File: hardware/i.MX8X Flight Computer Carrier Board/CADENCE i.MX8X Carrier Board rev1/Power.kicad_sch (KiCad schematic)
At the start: 64 parts, among them U1 LT8612, U2 LT8612, U3 TPS22975, U4 LT3115-1, U5 TLV71325PDQNR, U6 TLV71310PDQNR

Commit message: updated power schematic footprints for imx8x
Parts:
- U1, U2: footprint footprints:QFN-28_UDE_LTI -> LT8612:QFN-28_UDE_LTI
- U3: footprint (none) -> Footprints:DSG0008B
- U4: footprint (none) -> LTC3115EFE-1:CONV_LTC3115EFE-1_PBF
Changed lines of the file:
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@@
 			)
 		)
-		(property "Footprint" "footprints:QFN-28_UDE_LTI"
+		(property "Footprint" "LT8612:QFN-28_UDE_LTI"
 			(at 86.36 29.21 0)
 			(effects
@@
 			)
 		)
-		(property "Footprint" ""
+		(property "Footprint" "LTC3115EFE-1:CONV_LTC3115EFE-1_PBF"
 			(at 224.79 134.62 0)
 			(effects
@@
 			)
 		)
-		(property "Footprint" "footprints:QFN-28_UDE_LTI"
+		(property "Footprint" "LT8612:QFN-28_UDE_LTI"
 			(at 76.2 120.65 0)
 			(effects
@@
 			)
 		)
-		(property "Footprint" ""
+		(property "Footprint" "Footprints:DSG0008B"
 			(at 93.98 241.3 0)
 			(effects
@@
 			)
 		)
-		(property "Datasheet" ""
+		(property "Datasheet" "https://www.ti.com/lit/ds/symlink/tps22975.pdf?HQS=dis-dk-null-digikeymode-dsf-pf-null-wwe&ts=1774914142046&ref_url=https%253A%252F%252Fwww.ti.com%252Fgeneral%252Fdocs%252Fsuppproductinfo.tsp%253FdistId%253D10%2526gotoUrl%253Dhttps%253A%252F%252Fwww.ti.com%252Flit%252Fgpn%252Ftps22975"
 			(at 93.98 241.3 0)
 			(effects

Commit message: final rev1 schematic changes for phytec
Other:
- note added: "best high current low noise switching regulator with SEE test data"
- note added: "place left two LEDs close to power switch"
- note removed: "best high current low noise switching regulator with SEE test data (LT8613 failed at 1kRad tho yikes; maybe will be fine as LT8613 has a lot more fancy features)"
- note removed: "did this overnight, not sure if 100% good to go"
- note removed: "place these two close to power switch"

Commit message: updated imx8x footprints
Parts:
- C12, C13, C14, C15, C16, C18, C20, C21, C26, C31, C6, C7, C9: footprint (none) -> Capacitor_SMD:C_0603_1608Metric
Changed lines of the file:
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@@
 			)
 		)
-		(property "Footprint" ""
+		(property "Footprint" "Capacitor_SMD:C_0603_1608Metric"
 			(at 189.5348 146.05 0)
 			(effects
@@
 			)
 		)
-		(property "Footprint" ""
+		(property "Footprint" "Capacitor_SMD:C_0603_1608Metric"
 			(at 116.84 250.4948 0)
 			(effects
@@
 			)
 		)
-		(property "Footprint" ""
+		(property "Footprint" "Capacitor_SMD:C_0603_1608Metric"
 			(at 247.9548 166.37 0)
 			(effects
@@
 			)
 		)
-		(property "Footprint" ""
+		(property "Footprint" "Capacitor_SMD:C_0603_1608Metric"
 			(at 126.0348 158.75 0)
 			(effects
@@
 			)
 		)
-		(property "Footprint" ""
+		(property "Footprint" "Capacitor_SMD:C_0603_1608Metric"
 			(at 105.7148 124.46 0)
 			(effects
@@
 			)
 		)
-		(property "Footprint" ""
+		(property "Footprint" "Capacitor_SMD:C_0603_1608Metric"
 			(at 49.2252 259.08 0)
 			(effects
@@
 			)
 		)
-		(property "Footprint" ""
+		(property "Footprint" "Capacitor_SMD:C_0603_1608Metric"
 			(at 118.4148 243.84 0)
 			(effects
@@
 			)
 		)
-		(property "Footprint" ""
+		(property "Footprint" "Capacitor_SMD:C_0603_1608Metric"
 			(at 37.1348 152.4 0)
 			(effects
@@
 			)
 		)
-		(property "Footprint" ""
+		(property "Footprint" "Capacitor_SMD:C_0603_1608Metric"
 			(at 30.7848 152.4 0)
 			(effects
@@
 			)
 		)
-		(property "Footprint" ""
+		(property "Footprint" "Capacitor_SMD:C_0603_1608Metric"
 			(at 26.3652 137.16 0)
 			(effects
@@
 			)
 		)
-		(property "Footprint" ""
+		(property "Footprint" "Capacitor_SMD:C_0603_1608Metric"
 			(at 58.1152 259.08 0)
 			(effects
@@
 			)
 		)
-		(property "Footprint" ""
+		(property "Footprint" "Capacitor_SMD:C_0603_1608Metric"
 			(at 79.7052 264.16 0)
 			(effects
@@
 			)
 		)
-		(property "Footprint" ""
+		(property "Footprint" "Capacitor_SMD:C_0603_1608Metric"
 			(at 127.3048 243.84 0)
 			(effects

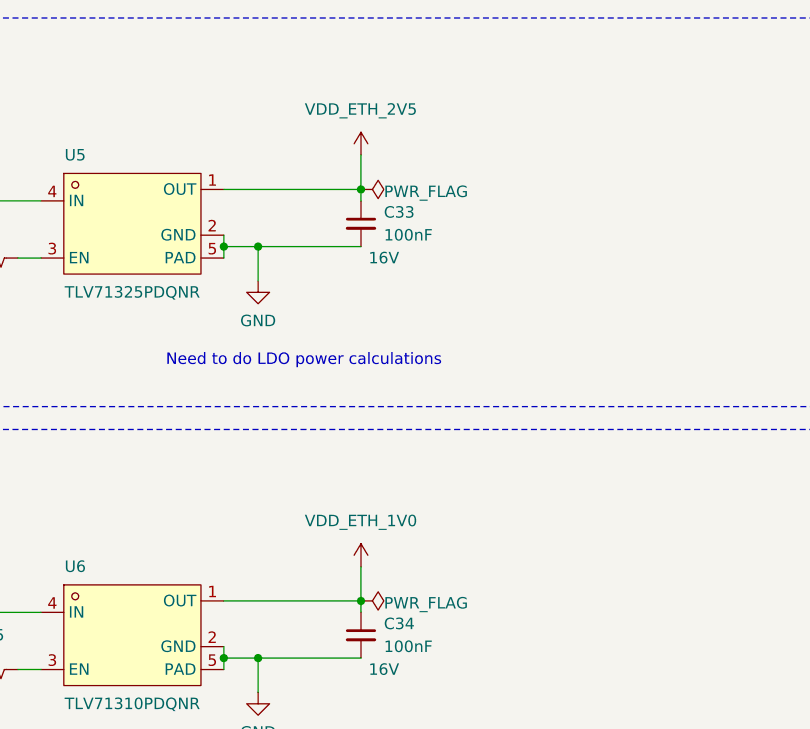
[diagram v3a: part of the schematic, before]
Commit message: Silly power net naming mistakes addressed
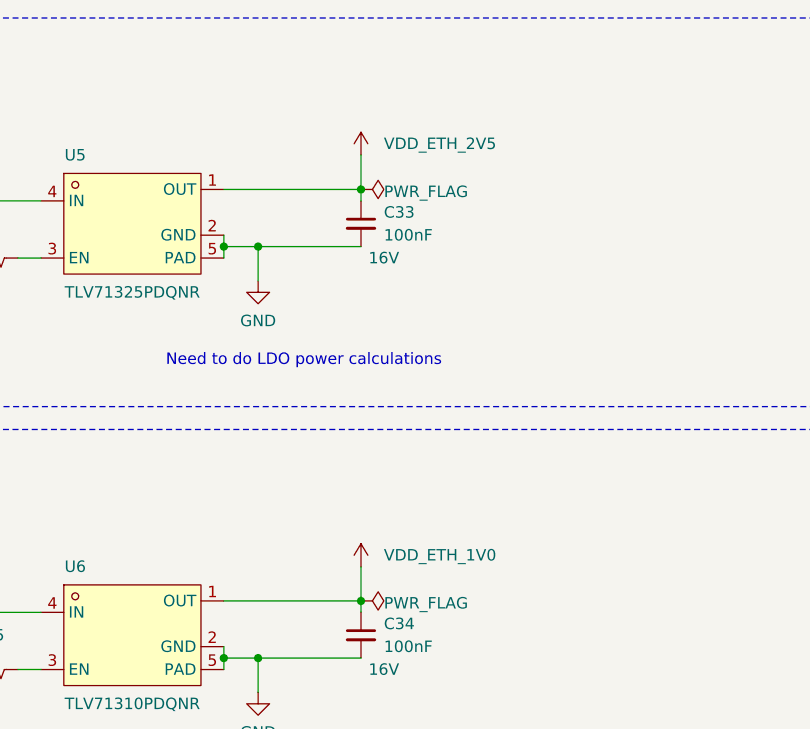
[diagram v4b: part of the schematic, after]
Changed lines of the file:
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@@
 		)
 		(property "Value" "VDD_ETH_1V0"
-			(at 261.62 68.58 0)
+			(at 264.16 72.3899 0)
 			(effects
 				(font
 					(size 1.27 1.27)
 				)
+				(justify left)
 			)
 		)
@@
 		)
 		(property "Value" "VDD_ETH_2V5"
-			(at 261.62 22.86 0)
+			(at 264.16 26.6699 0)
 			(effects
 				(font
 					(size 1.27 1.27)
 				)
+				(justify left)
 			)
 		)

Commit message: added footprints to imx8x, just need to finish usb, capacitors, and inductors
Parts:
- C10, C11, C17, C22, C29, C30, C32, C35, C36, C8: footprint (none) -> Capacitor_SMD:C_0603_1608Metric
- D1, D2, D3, D4, D5: footprint (none) -> LED_SMD:LED_0603_1608Metric
- R1, R10, R13, R14, R15, R16, R17, R18, R19, R2, R3, R4, R5, R6, R7, R8, R9: footprint (none) -> Resistor_SMD:R_0402_1005Metric
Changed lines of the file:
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@@
 			)
 		)
-		(property "Footprint" ""
+		(property "Footprint" "LED_SMD:LED_0603_1608Metric"
 			(at 218.44 214.63 0)
 			(effects
@@
 			)
 		)
-		(property "Footprint" ""
+		(property "Footprint" "Resistor_SMD:R_0402_1005Metric"
 			(at 55.372 68.58 90)
 			(effects
@@
 			)
 		)
-		(property "Footprint" ""
+		(property "Footprint" "Resistor_SMD:R_0402_1005Metric"
 			(at 111.252 60.96 90)
 			(effects
@@
 			)
 		)
-		(property "Footprint" ""
+		(property "Footprint" "Capacitor_SMD:C_0603_1608Metric"
 			(at 267.0048 143.51 0)
 			(effects
@@
 			)
 		)
-		(property "Footprint" ""
+		(property "Footprint" "Resistor_SMD:R_0402_1005Metric"
 			(at 119.888 162.56 90)
 			(effects
@@
 			)
 		)
-		(property "Footprint" ""
+		(property "Footprint" "Resistor_SMD:R_0402_1005Metric"
 			(at 125.222 176.53 90)
 			(effects
@@
 			)
 		)
-		(property "Footprint" ""
+		(property "Footprint" "Capacitor_SMD:C_0603_1608Metric"
 			(at 36.5252 45.72 0)
 			(effects
@@
 			)
 		)
-		(property "Footprint" ""
+		(property "Footprint" "LED_SMD:LED_0603_1608Metric"
 			(at 236.22 214.63 0)
 			(effects
@@
 			)
 		)
-		(property "Footprint" ""
+		(property "Footprint" "Resistor_SMD:R_0402_1005Metric"
 			(at 263.652 223.52 90)
 			(effects
@@
 			)
 		)
-		(property "Footprint" ""
+		(property "Footprint" "Resistor_SMD:R_0402_1005Metric"
 			(at 249.682 223.52 90)
 			(effects
@@
 			)
 		)
-		(property "Footprint" ""
+		(property "Footprint" "Capacitor_SMD:C_0603_1608Metric"
 			(at 47.2948 60.96 0)
 			(effects
@@
 			)
 		)
-		(property "Footprint" ""
+		(property "Footprint" "Resistor_SMD:R_0402_1005Metric"
 			(at 204.978 168.91 90)
 			(effects
@@
 			)
 		)
-		(property "Footprint" ""
+		(property "Footprint" "Capacitor_SMD:C_0603_1608Metric"
 			(at 214.9348 125.73 0)
 			(effects
@@
 			)
 		)
-		(property "Footprint" ""
+		(property "Footprint" "Resistor_SMD:R_0402_1005Metric"
 			(at 216.662 223.52 90)
 			(effects
@@
 			)
 		)
-		(property "Footprint" ""
+		(property "Footprint" "Capacitor_SMD:C_0603_1608Metric"
 			(at 40.9448 60.96 0)
 			(effects
@@
 			)
 		)
-		(property "Footprint" ""
+		(property "Footprint" "Resistor_SMD:R_0402_1005Metric"
 			(at 281.178 147.32 90)
 			(effects
@@
 			)
 		)
-		(property "Footprint" ""
+		(property "Footprint" "Capacitor_SMD:C_0603_1608Metric"
 			(at 255.27 155.9052 0)
 			(effects
@@
 			)
 		)
-		(property "Footprint" ""
+		(property "Footprint" "Capacitor_SMD:C_0603_1608Metric"
 			(at 232.7148 125.73 0)
 			(effects
@@
 			)
 		)
-		(property "Footprint" ""
+		(property "Footprint" "Resistor_SMD:R_0402_1005Metric"
 			(at 247.65 153.162 90)
 			(effects
@@
 			)
 		)
-		(property "Footprint" ""
+		(property "Footprint" "LED_SMD:LED_0603_1608Metric"
 			(at 251.46 214.63 0)
 			(effects
@@
 			)
 		)
-		(property "Footprint" ""
+		(property "Footprint" "Resistor_SMD:R_0402_1005Metric"
 			(at 281.178 167.64 90)
 			(effects
@@
 			)
 		)
-		(property "Footprint" ""
+		(property "Footprint" "Resistor_SMD:R_0402_1005Metric"
 			(at 131.318 85.09 90)
 			(effects
@@
 			)
 		)
-		(property "Footprint" ""
+		(property "Footprint" "Resistor_SMD:R_0402_1005Metric"
 			(at 122.428 71.12 90)
 			(effects
@@
 			)
 		)
-		(property "Footprint" ""
+		(property "Footprint" "LED_SMD:LED_0603_1608Metric"
 			(at 190.5 214.63 0)
 			(effects
@@
 			)
 		)
-		(property "Footprint" ""
+		(property "Footprint" "LED_SMD:LED_0603_1608Metric"
 			(at 265.43 214.63 0)
 			(effects
@@
 			)
 		)
-		(property "Footprint" ""
+		(property "Footprint" "Resistor_SMD:R_0402_1005Metric"
 			(at 45.212 160.02 90)
 			(effects
@@
 			)
 		)
-		(property "Footprint" ""
+		(property "Footprint" "Resistor_SMD:R_0402_1005Metric"
 			(at 188.722 223.52 90)
 			(effects
@@
 			)
 		)
-		(property "Footprint" ""
+		(property "Footprint" "Capacitor_SMD:C_0603_1608Metric"
 			(at 115.8748 33.02 0)
 			(effects
@@
 			)
 		)
-		(property "Footprint" ""
+		(property "Footprint" "Resistor_SMD:R_0402_1005Metric"
 			(at 234.442 223.52 90)
 			(effects
@@
 			)
 		)
-		(property "Footprint" ""
+		(property "Footprint" "Capacitor_SMD:C_0603_1608Metric"
 			(at 291.1348 143.51 0)
 			(effects
@@
 			)
 		)
-		(property "Footprint" ""
+		(property "Footprint" "Resistor_SMD:R_0402_1005Metric"
 			(at 293.878 154.94 90)
 			(effects
@@
 			)
 		)
-		(property "Footprint" ""
+		(property "Footprint" "Capacitor_SMD:C_0603_1608Metric"
 			(at 128.5748 67.31 0)
 			(effects

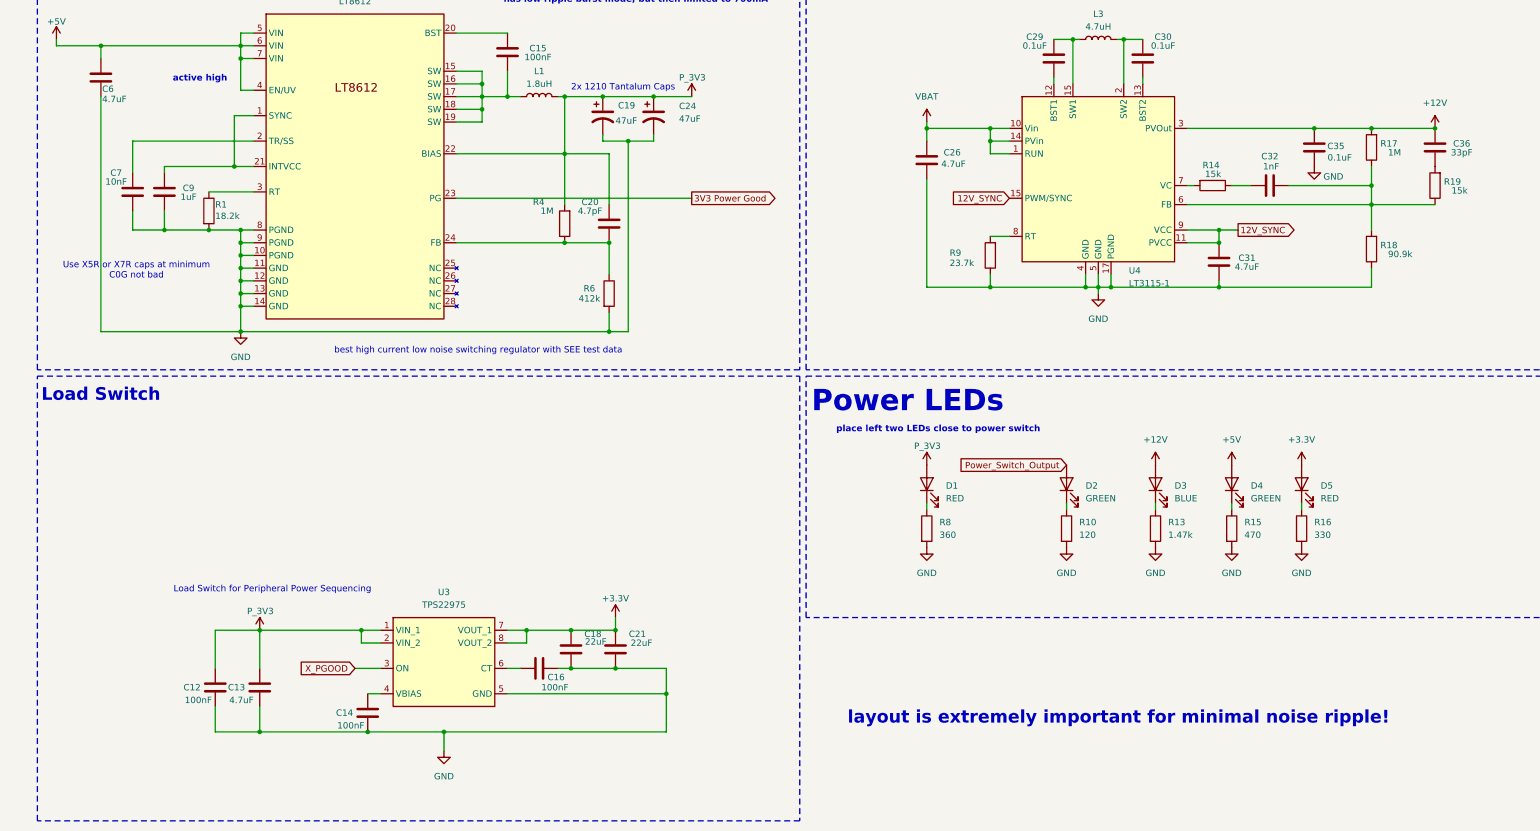
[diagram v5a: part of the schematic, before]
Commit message: reorged pin definitions page
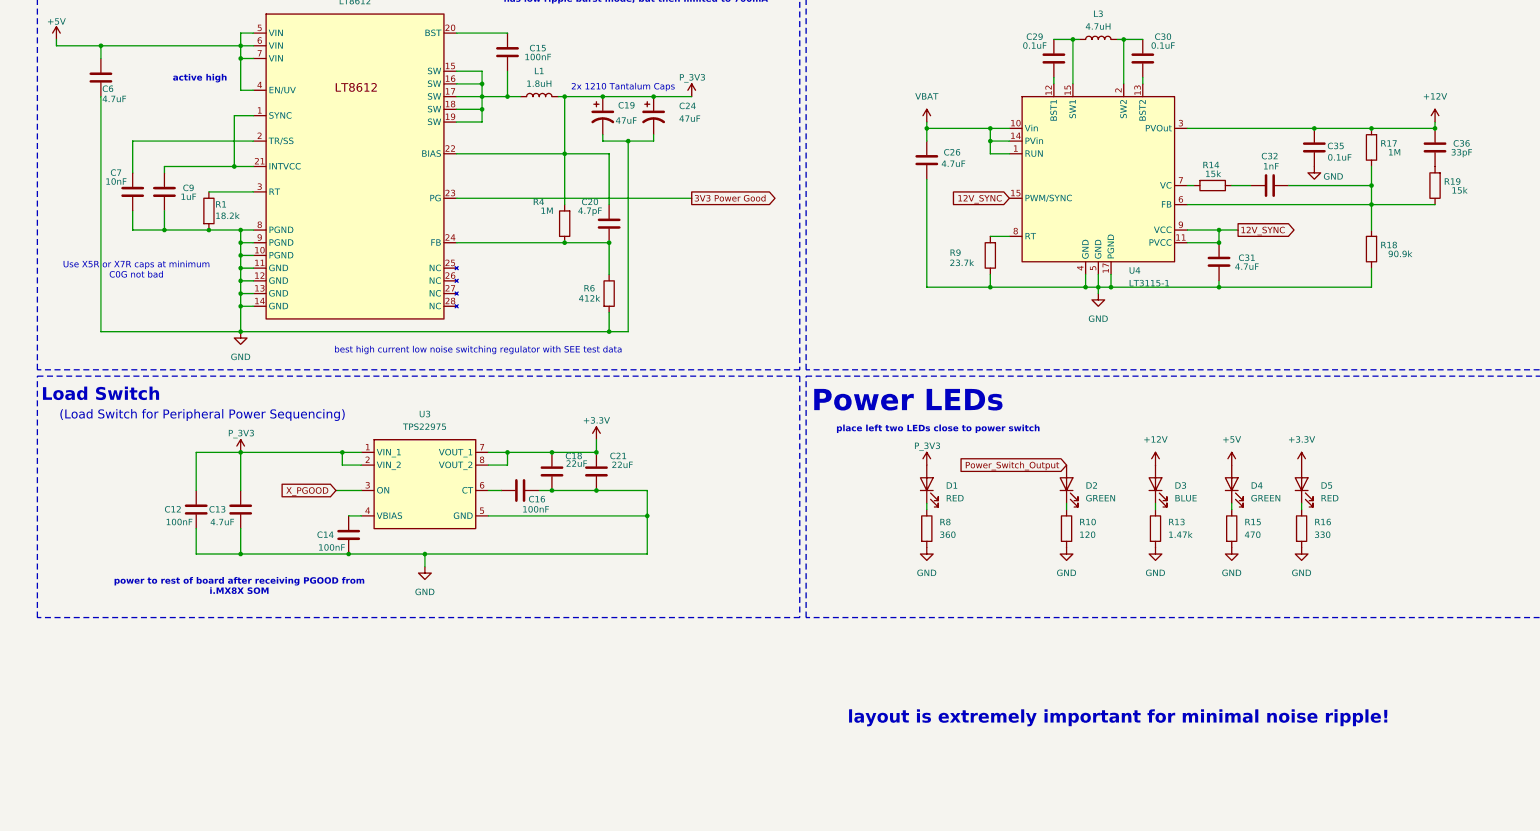
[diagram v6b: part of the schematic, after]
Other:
- note added: "(Load Switch for Peripheral Power Sequencing)"
- note added: "power to rest of board after receiving PGOOD from i.MX8X SOM"
- note removed: "Load Switch for Peripheral Power Sequencing"
- moved on the sheet: C12, C13, C14, C16, C18, C21, U3

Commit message: Finished footprints- Double check usbs
Only thing i didn't touch was watchdogs. That might still need to be changed.
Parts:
- C10, C12, C14, C15, C16, C17, C20, C22, C27, C28, C32, C33, C34, C36, C7: footprint Capacitor_SMD:C_0603_1608Metric -> Capacitor_SMD:C_0402_1005Metric
- C18, C21: footprint Capacitor_SMD:C_0603_1608Metric -> Capacitor_SMD:C_0805_2012Metric
- C19, C23, C24, C25: footprint (none) -> Capacitor_SMD:C_0805_2012Metric
- L1: footprint (none) -> Footprints:IND-SMD_L6.6-W6.4-P4.04_XAL6030-182MEC
- L2: footprint (none) -> Footprints:IND-SMD_L10.9-W10.0
- L3: footprint (none) -> Footprints:IND-SMD_L7.0-W6.6
- R17, R4, R5: footprint Resistor_SMD:R_0402_1005Metric -> Resistor_SMD:R_0603_1608Metric
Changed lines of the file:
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@@
 			)
 		)
-		(property "Footprint" "Capacitor_SMD:C_0603_1608Metric"
+		(property "Footprint" "Capacitor_SMD:C_0402_1005Metric"
 			(at 261.62 35.56 0)
 			(effects
@@
 			)
 		)
-		(property "Footprint" ""
+		(property "Footprint" "Capacitor_SMD:C_0805_2012Metric"
 			(at 125.73 140.97 0)
 			(effects
@@
 			)
 		)
-		(property "Footprint" "Capacitor_SMD:C_0603_1608Metric"
+		(property "Footprint" "Capacitor_SMD:C_0402_1005Metric"
 			(at 113.03 214.9348 0)
 			(effects
@@
 			)
 		)
-		(property "Footprint" "Resistor_SMD:R_0402_1005Metric"
+		(property "Footprint" "Resistor_SMD:R_0603_1608Metric"
 			(at 119.888 162.56 90)
 			(effects
@@
 			)
 		)
-		(property "Footprint" ""
+		(property "Footprint" "Capacitor_SMD:C_0805_2012Metric"
 			(at 146.05 49.53 0)
 			(effects
@@
 			)
 		)
-		(property "Footprint" "Capacitor_SMD:C_0603_1608Metric"
+		(property "Footprint" "Capacitor_SMD:C_0402_1005Metric"
 			(at 126.0348 158.75 0)
 			(effects
@@
 			)
 		)
-		(property "Footprint" ""
+		(property "Footprint" "Footprints:IND-SMD_L6.6-W6.4-P4.04_XAL6030-182MEC"
 			(at 113.03 137.16 0)
 			(effects
@@
 			)
 		)
-		(property "Footprint" "Capacitor_SMD:C_0603_1608Metric"
+		(property "Footprint" "Capacitor_SMD:C_0402_1005Metric"
 			(at 105.7148 124.46 0)
 			(effects
@@
 			)
 		)
-		(property "Footprint" "Capacitor_SMD:C_0603_1608Metric"
+		(property "Footprint" "Capacitor_SMD:C_0402_1005Metric"
 			(at 201.93 83.82 0)
 			(effects
@@
 			)
 		)
-		(property "Footprint" "Capacitor_SMD:C_0603_1608Metric"
+		(property "Footprint" "Capacitor_SMD:C_0402_1005Metric"
 			(at 261.62 81.28 0)
 			(effects
@@
 			)
 		)
-		(property "Footprint" ""
+		(property "Footprint" "Capacitor_SMD:C_0805_2012Metric"
 			(at 135.89 140.97 0)
 			(effects
@@
 			)
 		)
-		(property "Footprint" ""
+		(property "Footprint" "Footprints:IND-SMD_L7.0-W6.6"
 			(at 224.79 125.73 0)
 			(effects
@@
 			)
 		)
-		(property "Footprint" "Capacitor_SMD:C_0603_1608Metric"
+		(property "Footprint" "Capacitor_SMD:C_0402_1005Metric"
 			(at 40.9448 60.96 0)
 			(effects
@@
 			)
 		)
-		(property "Footprint" "Resistor_SMD:R_0402_1005Metric"
+		(property "Footprint" "Resistor_SMD:R_0603_1608Metric"
 			(at 281.178 147.32 90)
 			(effects
@@
 			)
 		)
-		(property "Footprint" "Capacitor_SMD:C_0603_1608Metric"
+		(property "Footprint" "Capacitor_SMD:C_0402_1005Metric"
 			(at 255.27 155.9052 0)
 			(effects
@@
 			)
 		)
-		(property "Footprint" "Capacitor_SMD:C_0603_1608Metric"
+		(property "Footprint" "Capacitor_SMD:C_0402_1005Metric"
 			(at 45.4152 223.52 0)
 			(effects
@@
 			)
 		)
-		(property "Footprint" "Capacitor_SMD:C_0603_1608Metric"
+		(property "Footprint" "Capacitor_SMD:C_0805_2012Metric"
 			(at 114.6048 208.28 0)
 			(effects
@@
 			)
 		)
-		(property "Footprint" "Capacitor_SMD:C_0603_1608Metric"
+		(property "Footprint" "Capacitor_SMD:C_0402_1005Metric"
 			(at 30.7848 152.4 0)
 			(effects
@@
 			)
 		)
-		(property "Footprint" "Capacitor_SMD:C_0603_1608Metric"
+		(property "Footprint" "Capacitor_SMD:C_0402_1005Metric"
 			(at 201.93 38.1 0)
 			(effects
@@
 			)
 		)
-		(property "Footprint" "Resistor_SMD:R_0402_1005Metric"
+		(property "Footprint" "Resistor_SMD:R_0603_1608Metric"
 			(at 122.428 71.12 90)
 			(effects
@@
 			)
 		)
-		(property "Footprint" "Capacitor_SMD:C_0603_1608Metric"
+		(property "Footprint" "Capacitor_SMD:C_0402_1005Metric"
 			(at 115.8748 33.02 0)
 			(effects
@@
 			)
 		)
-		(property "Footprint" ""
+		(property "Footprint" "Footprints:IND-SMD_L10.9-W10.0"
 			(at 124.46 45.72 0)
 			(effects
@@
 			)
 		)
-		(property "Footprint" "Capacitor_SMD:C_0603_1608Metric"
+		(property "Footprint" "Capacitor_SMD:C_0402_1005Metric"
 			(at 75.8952 228.6 0)
 			(effects
@@
 			)
 		)
-		(property "Footprint" "Capacitor_SMD:C_0603_1608Metric"
+		(property "Footprint" "Capacitor_SMD:C_0402_1005Metric"
 			(at 291.1348 143.51 0)
 			(effects
@@
 			)
 		)
-		(property "Footprint" ""
+		(property "Footprint" "Capacitor_SMD:C_0805_2012Metric"
 			(at 135.89 49.53 0)
 			(effects
@@
 			)
 		)
-		(property "Footprint" "Capacitor_SMD:C_0603_1608Metric"
+		(property "Footprint" "Capacitor_SMD:C_0805_2012Metric"
 			(at 123.4948 208.28 0)
 			(effects
@@
 			)
 		)
-		(property "Footprint" "Capacitor_SMD:C_0603_1608Metric"
+		(property "Footprint" "Capacitor_SMD:C_0402_1005Metric"
 			(at 128.5748 67.31 0)
 			(effects

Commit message: connection changes, debug headers, fixing critical issues
-finished debug/utility header pin section (may have to reassign some gpios again tho)
- added can bus transceiver and connection to satnogs
- reassigned/ ensured no i2c address conflict
- resolved critical error in LTC-3115 power regulator symbol where output power was shorted to sync pin
-resolved critical symbol issue in which imx8x som power good symbol shorted to gnd, which would result in nonfunctional board & 2 jtag pins shorted

to do:
- assign gpio to a load switch
- resolve erc issues
- footprint check (shunt resistor change, some new ics need footprints, cmos image sensor 8 pin jst connector, etc)
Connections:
- net 12V_SYNC: now also U4.16 (PWM/SYNC); no longer U4.15 (SW1)
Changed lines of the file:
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@@
 		(pin "17"
 		)
-		(pin "15"
+		(pin "16"
 		)
 		(pin "15"
